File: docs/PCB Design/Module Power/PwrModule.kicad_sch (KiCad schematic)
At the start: 4 parts, among them J11 Conn_02x05_Top_Bottom, J14 Conn_02x04_Counter_Clockwise

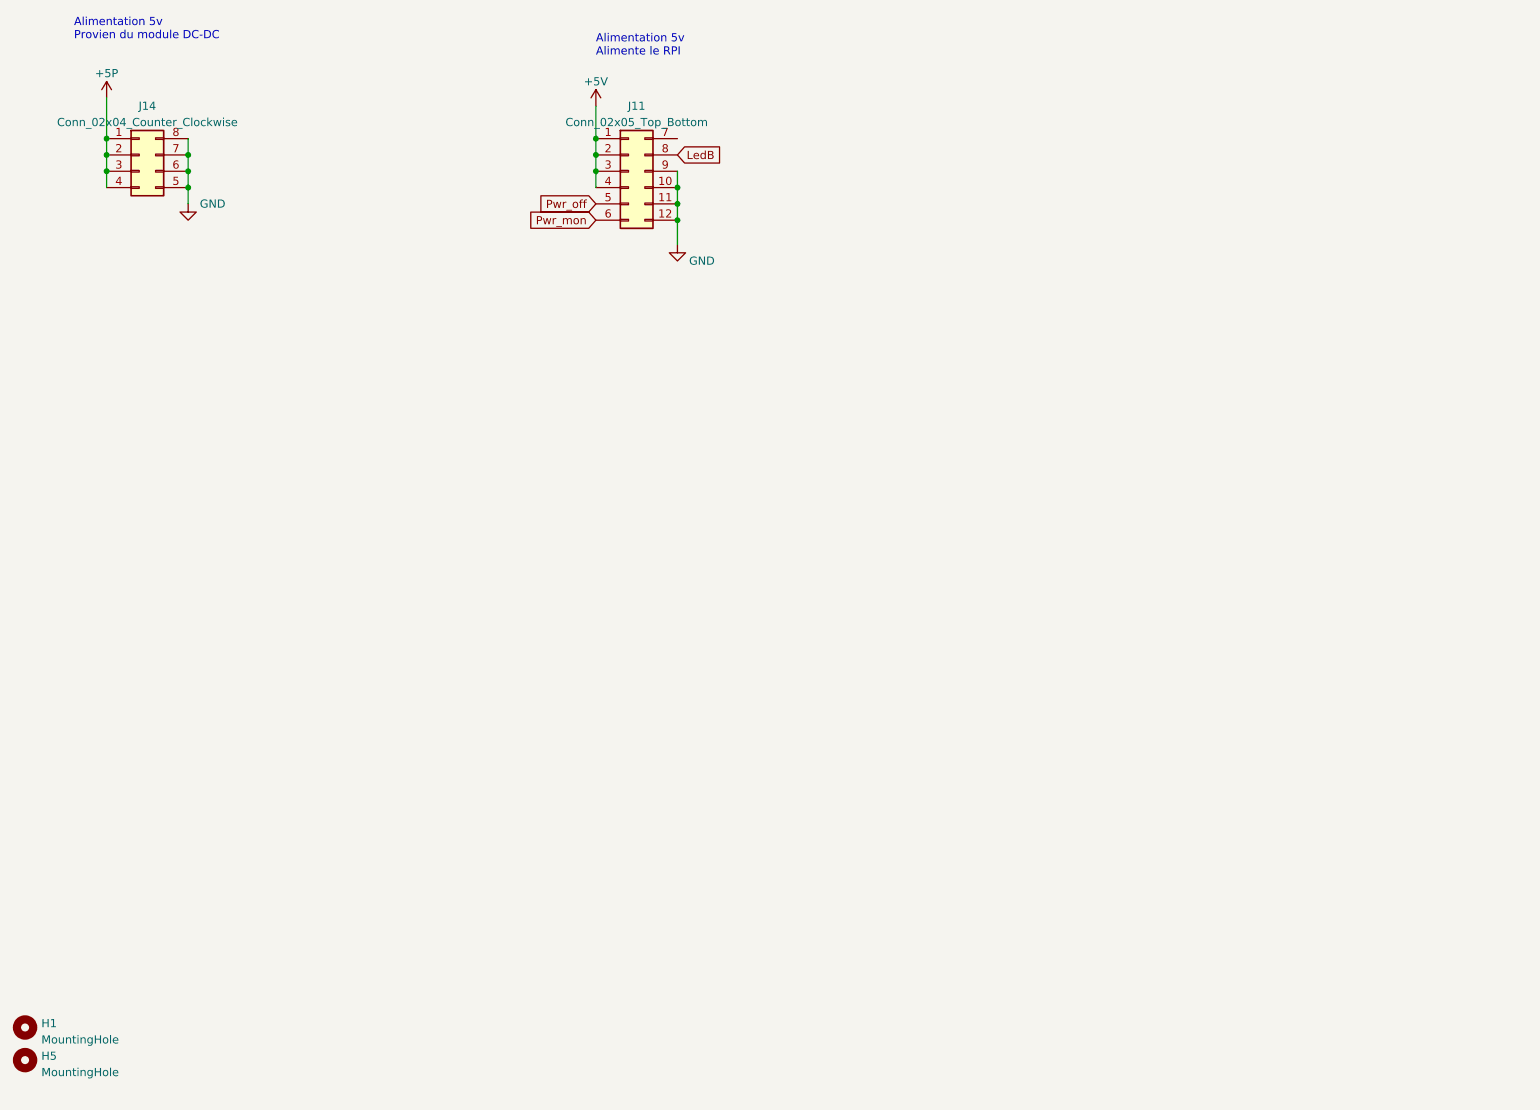
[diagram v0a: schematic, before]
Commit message: module power 1.0 module bypass 1.1
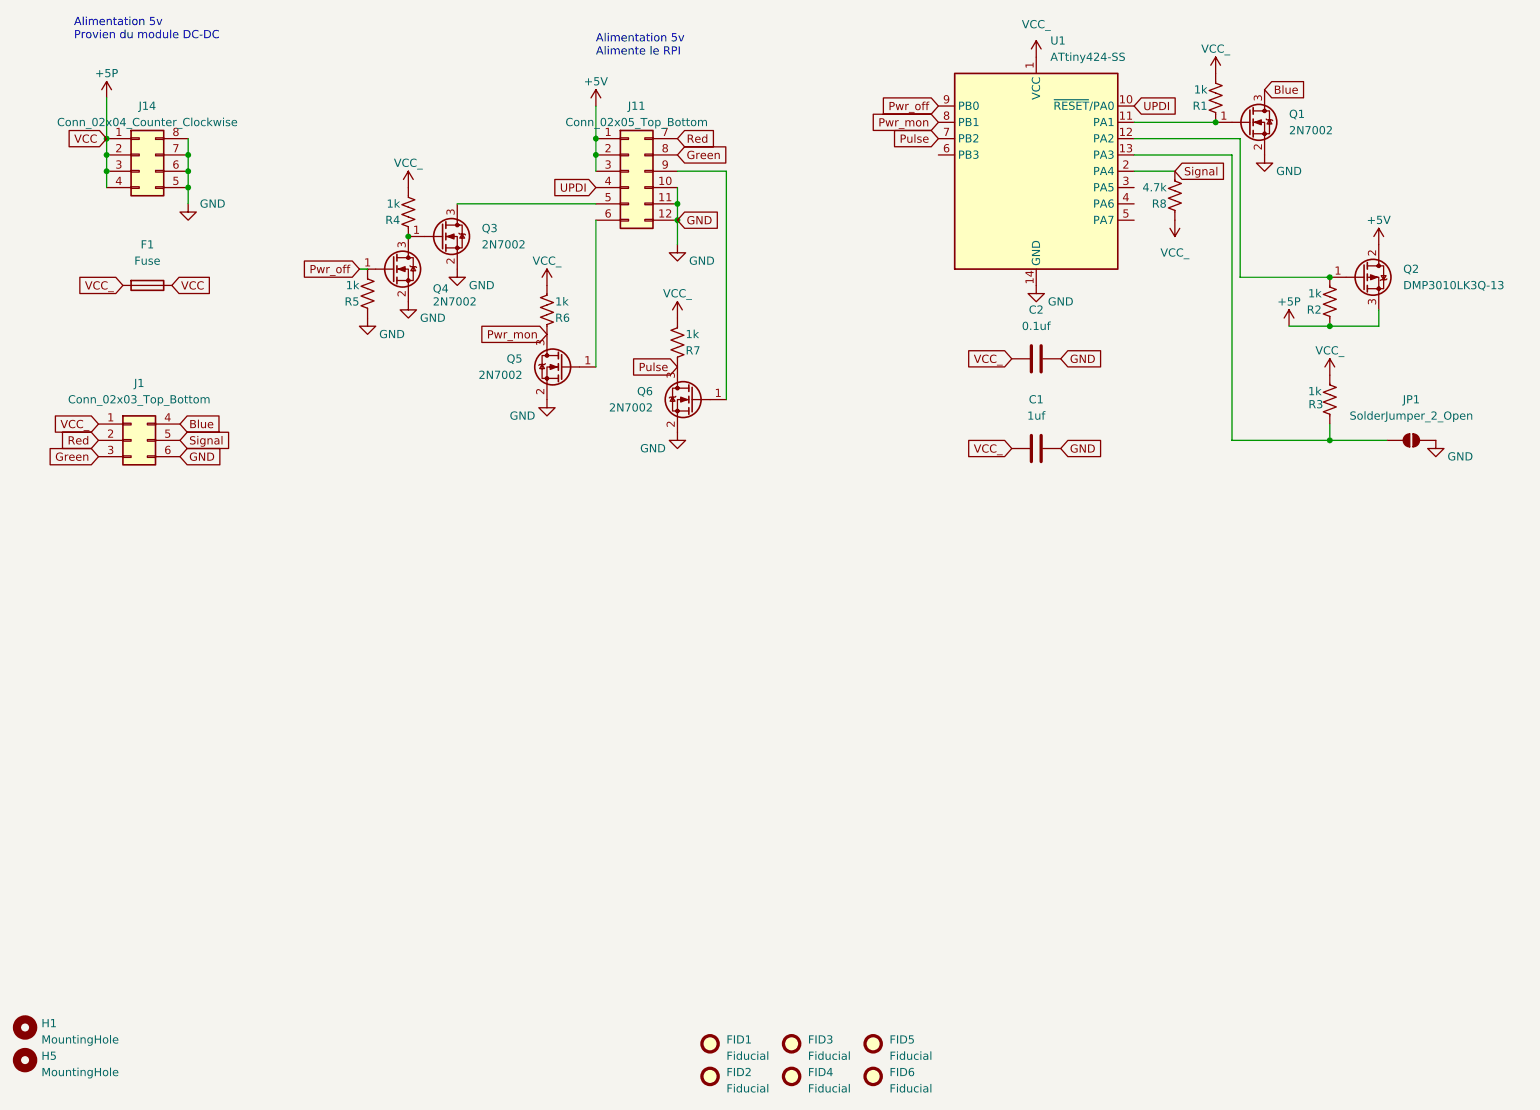
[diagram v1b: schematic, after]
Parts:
- added C1: 1uf, Capacitor_SMD:C_1206_3216Metric, symbol Device:C
- added C2: 0.1uf, Capacitor_SMD:C_1206_3216Metric, symbol Device:C
- added F1: Fuse, Fuse:Fuse_1206_3216Metric, symbol Device:Fuse
- added FID1, FID2, FID3, FID4, FID5, FID6: Fiducial, Fiducial:Fiducial_0.75mm_Mask2.25mm, symbol Mechanical:Fiducial
- added J1: Conn_02x03_Top_Bottom, Connector_IDC:IDC-Header_2x03_P2.54mm_Vertical, symbol Connector_Generic:Conn_02x03_Top_Bottom
- added JP1: SolderJumper_2_Open, Jumper:SolderJumper-2_P1.3mm_Open_TrianglePad1.0x1.5mm, symbol Jumper:SolderJumper_2_Open
- added Q1, Q3, Q4, Q5, Q6: 2N7002, Package_TO_SOT_SMD:SOT-23, symbol Transistor_FET:2N7002
- added Q2: DMP3010LK3Q-13, Package_TO_SOT_SMD:TO-252-2, symbol Transistor_FET:SUD19P06-60
- added R1, R2, R3, R4, R5, R6, R7: 1k, Resistor_SMD:R_1206_3216Metric, symbol Device:R_US
- added R8: 4.7k, Resistor_SMD:R_1206_3216Metric, symbol Device:R_US
- added U1: ATtiny424-SS, Package_SO:SOIC-14_3.9x8.7mm_P1.27mm, symbol MCU_Microchip_ATtiny:ATtiny424-SS
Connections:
- net +5P: now also F1.1, Q2.3 (S), R2.1
- net +5V: now also Q2.2 (D); no longer J11.4 (Pin_4)
- net GND: now also C1.1, C2.1, J1.6 (Pin_6), JP1.2 (B), Q1.2 (S), Q3.2 (S), Q4.2 (S), Q5.2 (S), Q6.2 (S), R5.1, U1.14 (GND); no longer J11.9 (Pin_9)
- net Pwr_mon: now also Q5.3 (D), R6.1, U1.8 (PB1); no longer J11.6 (Pin_6)
- net Pwr_off: now also Q4.1 (G), R5.2, U1.9 (PB0); no longer J11.5 (Pin_5)
- net Red: now reaches J11.7 (Pin_7)
- net Red: now also J1.2 (Pin_2)
- net LedB renamed Green
- net Green: now also J1.3 (Pin_3)
- new net: Q2.1 (G), R2.2, U1.12 (PA2)
- new net: Q3.1 (G), Q4.3 (D), R4.1
- new net: J11.5 (Pin_5), Q3.3 (D)
- new net: Q1.1 (G), R1.1, U1.11 (PA1)
- new net: J11.6 (Pin_6), Q5.1 (G)
- new net: J11.9 (Pin_9), Q6.1 (G)
- new net: JP1.1 (A), R3.1, U1.13 (PA3)
- new net Blue: J1.4 (Pin_4), Q1.3 (D)
- new net Pulse: Q6.3 (D), R7.1, U1.7 (PB2)
- new net Signal: J1.5 (Pin_5), R8.2, U1.2 (PA4)
- new net UPDI: J11.4 (Pin_4), U1.10 (~{RESET}/PA0)
- new net VCC_: C1.2, C2.2, F1.2, J1.1 (Pin_1), R1.2, R3.2, R4.2, R6.2, R7.2, R8.1, U1.1 (VCC)
